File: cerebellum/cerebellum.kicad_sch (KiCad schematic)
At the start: 8 parts, among them J1 GPIO, U1 CAT24C256, U2 POLOLU_TB6612_CARRIER

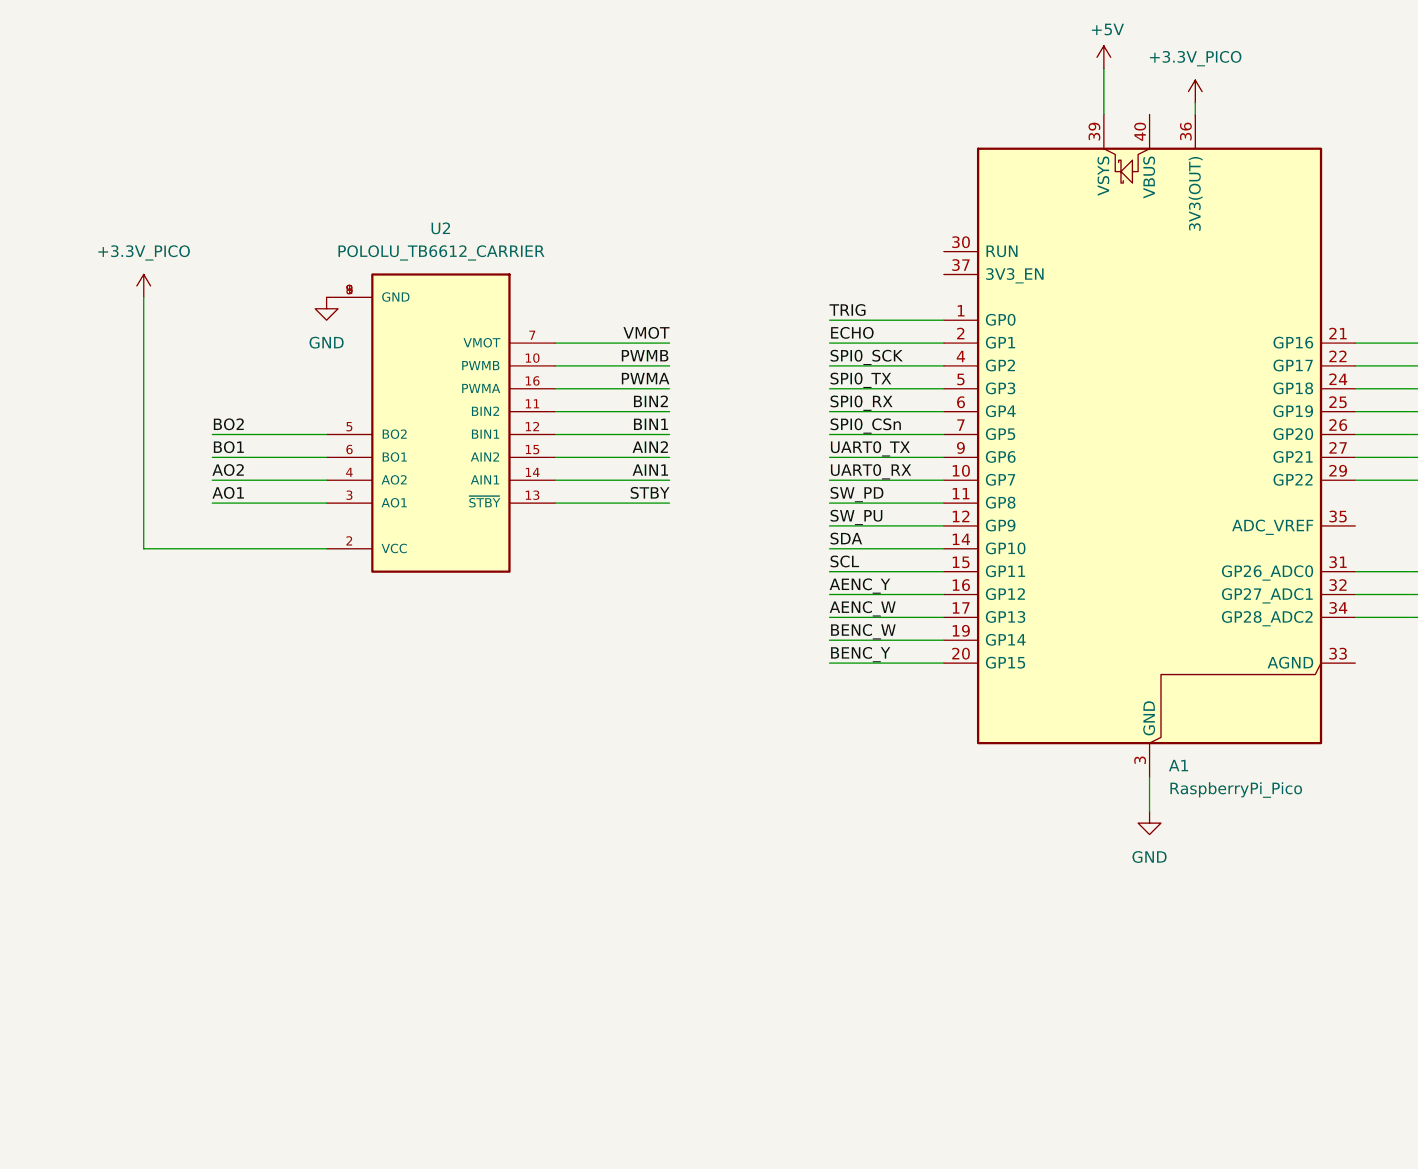
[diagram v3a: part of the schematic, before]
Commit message: update schematic
added HC-SR04
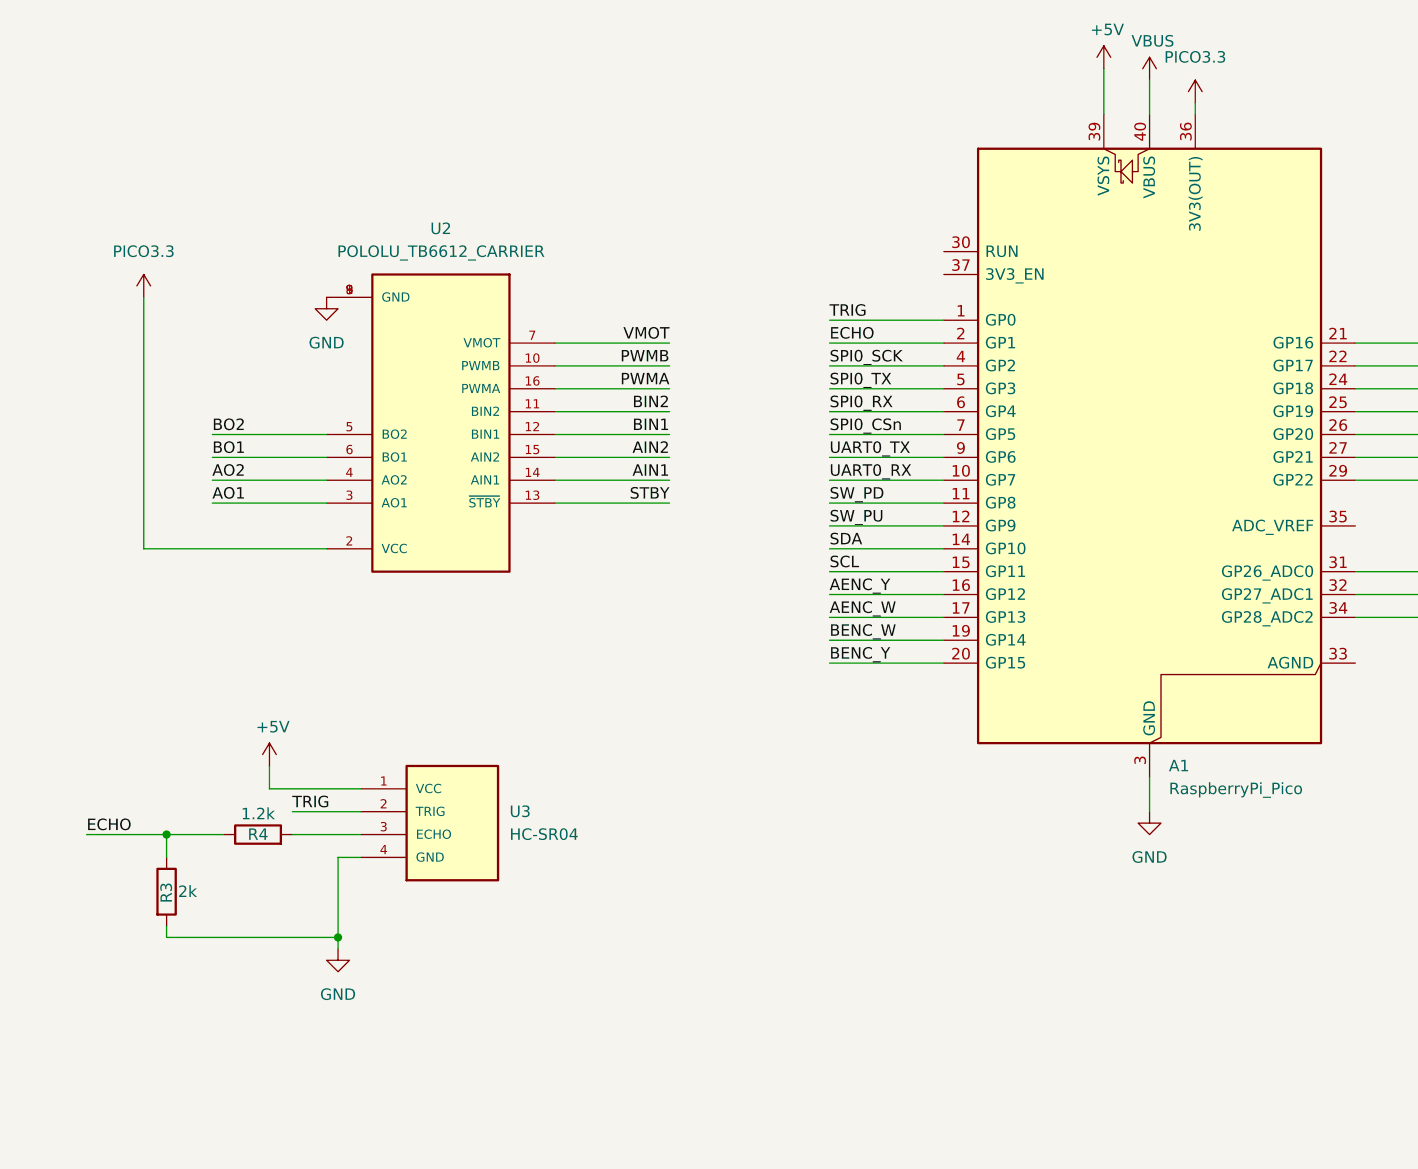
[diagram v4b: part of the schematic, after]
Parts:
- added R3: 2k, symbol Device:R
- added R4: 1.2k, symbol Device:R
- added U3: HC-SR04, HC-SR04:XCVR_HC-SR04, symbol HC-SR04:HC-SR04
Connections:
- net +5V: now also U3.1 (VCC)
- net ECHO: now also R3.1, R4.1
- net GND: now also R3.2, U3.4 (GND)
- net TRIG: now also U3.2 (TRIG)
- net VBUS: now reaches A1.40 (VBUS)
- net +3.3V_PICO renamed PICO3.3
- new net: R4.2, U3.3 (ECHO)

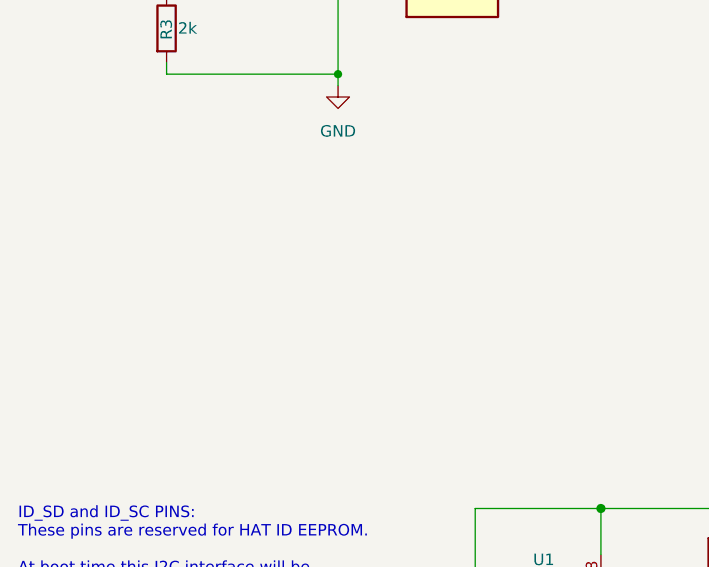
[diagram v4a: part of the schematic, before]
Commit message: update schematic
added RGB LED
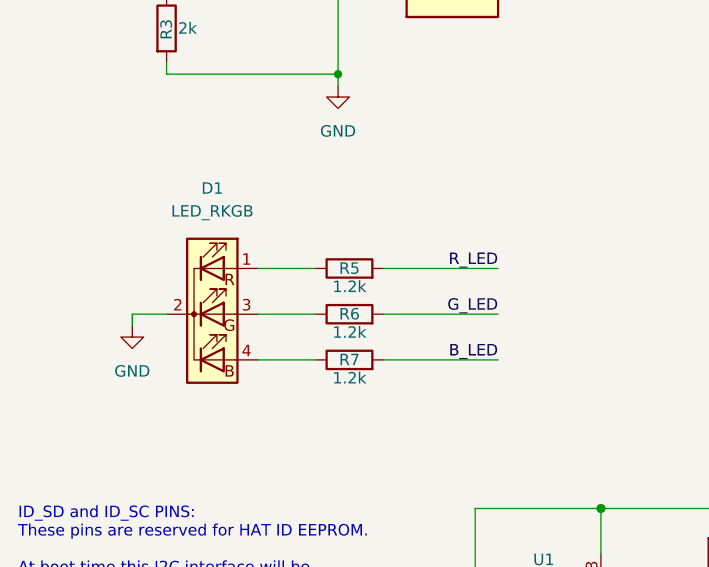
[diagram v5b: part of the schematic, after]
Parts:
- added D1: LED_RKGB, symbol Device:LED_RKGB
- added R5, R6, R7: 1.2k, symbol Device:R
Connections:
- net B_LED: now also R7.2
- net GND: now also D1.2 (K)
- net G_LED: now also R6.2
- net R_LED: now also R5.2
- new net: D1.1 (RA), R5.1
- new net: D1.3 (GA), R6.1
- new net: D1.4 (BA), R7.1

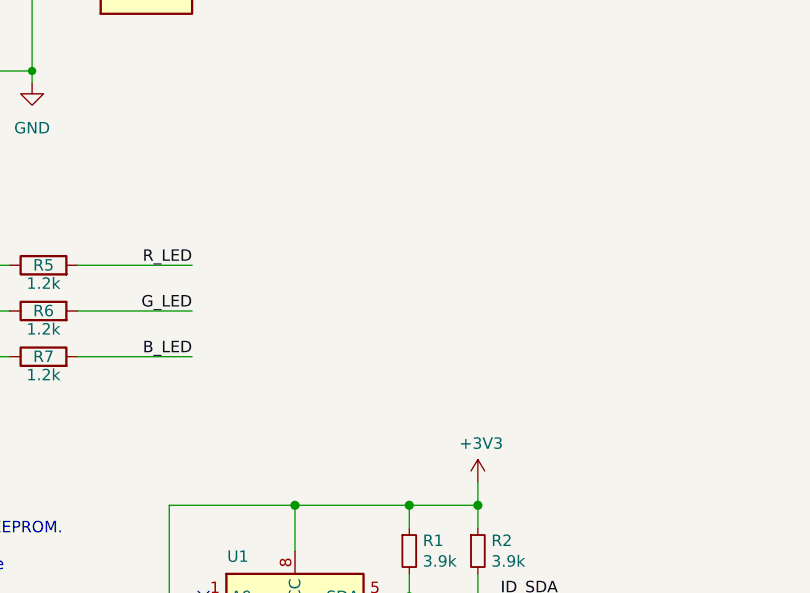
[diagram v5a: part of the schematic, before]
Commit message: update schematic
added pull-up and pull-down switches
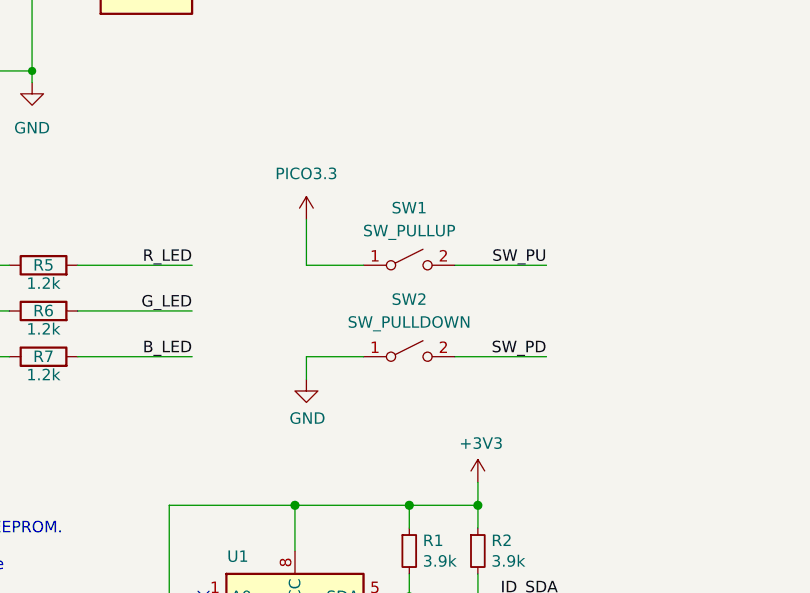
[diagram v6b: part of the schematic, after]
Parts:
- added SW1: SW_PULLUP, symbol Switch:SW_SPST
- added SW2: SW_PULLDOWN, symbol Switch:SW_SPST
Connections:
- net GND: now also SW2.1 (A)
- net PICO3.3: now also SW1.1 (A)
- net SW_PD: now also SW2.2 (B)
- net SW_PU: now also SW1.2 (B)

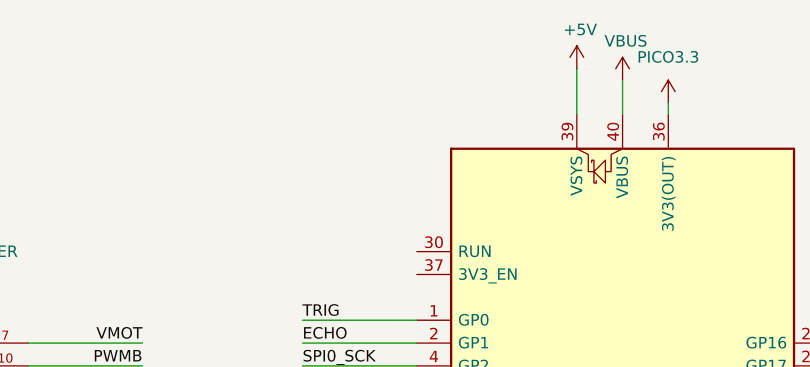
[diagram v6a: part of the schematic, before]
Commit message: update schematic
added spdt switch to power pico
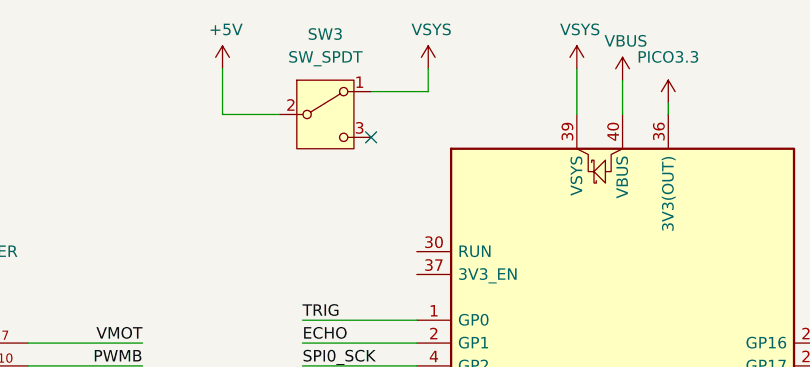
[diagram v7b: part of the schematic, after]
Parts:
- added SW3: SW_SPDT, symbol Switch:SW_SPDT
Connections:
- net +5V: now also SW3.2 (B); no longer A1.39 (VSYS)
- new net VSYS: A1.39 (VSYS), SW3.1 (A)
- no-connect marks 3 -> 4
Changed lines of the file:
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@@
 		(at 71.12 180.34)
 	)
+	(no_connect
+		(at 114.3 27.94)
+	)
 	(wire
 		(pts
@@
 	(wire
 		(pts
+			(xy 120.65 22.86) (xy 120.65 20.32)
+		)
+		(stroke
+			(width 0)
+			(type default)
+		)
+	)
+	(wire
+		(pts
 			(xy 147.32 25.4) (xy 147.32 24.13)
 		)
@@
 	(wire
 		(pts
+			(xy 97.79 25.4) (xy 104.14 25.4)
+		)
+		(stroke
+			(width 0)
+			(type default)
+		)
+	)
+	(wire
+		(pts
 			(xy 57.15 138.43) (xy 69.85 138.43)
 		)
@@
 	(wire
 		(pts
+			(xy 97.79 20.32) (xy 97.79 25.4)
+		)
+		(stroke
+			(width 0)
+			(type default)
+		)
+	)
+	(wire
+		(pts
 			(xy 248.92 68.58) (xy 246.38 68.58)
 		)
@@
 	(wire
 		(pts
+			(xy 114.3 22.86) (xy 120.65 22.86)
+		)
+		(stroke
+			(width 0)
+			(type default)
+		)
+	)
+	(wire
+		(pts
 			(xy 81.28 185.42) (xy 81.28 187.96)
 		)
@@
 	(symbol
 		(lib_id "power:+5V")
-		(at 137.16 20.32 0)
+		(at 97.79 20.32 0)
 		(unit 1)
 		(exclude_from_sim no)
@@
 		(dnp no)
 		(property "Reference" "#PWR011"
-			(at 137.16 24.13 0)
+			(at 97.79 24.13 0)
 			(effects
 				(font
@@
 		)
 		(property "Value" "+5V"
-			(at 137.5283 15.9956 0)
+			(at 98.1583 15.9956 0)
 			(effects
 				(font
@@
 		)
 		(property "Footprint" ""
-			(at 137.16 20.32 0)
+			(at 97.79 20.32 0)
 			(effects
 				(font
@@
 		)
 		(property "Datasheet" ""
-			(at 137.16 20.32 0)
+			(at 97.79 20.32 0)
 			(effects
 				(font
@@
 		)
 		(property "Description" ""
-			(at 137.16 20.32 0)
+			(at 97.79 20.32 0)
 			(effects
 				(font
@@
 	)
 	(symbol
+		(lib_id "power:+5V")
+		(at 120.65 20.32 0)
+		(unit 1)
+		(exclude_from_sim no)
+		(in_bom yes)
+		(on_board yes)
+		(dnp no)
+		(property "Reference" "#PWR020"
+			(at 120.65 24.13 0)
+			(effects
+				(font
+					(size 1.27 1.27)
+				)
+				(hide yes)
+			)
+		)
+		(property "Value" "VSYS"
+			(at 121.0183 15.9956 0)
+			(effects
+				(font
+					(size 1.27 1.27)
+				)
+			)
+		)
+		(property "Footprint" ""
+			(at 120.65 20.32 0)
+			(effects
+				(font
+					(size 1.27 1.27)
+				)
+			)
+		)
+		(property "Datasheet" ""
+			(at 120.65 20.32 0)
+			(effects
+				(font
+					(size 1.27 1.27)
+				)
+			)
+		)
+		(property "Description" ""
+			(at 120.65 20.32 0)
+			(effects
+				(font
+					(size 1.27 1.27)
+				)
+			)
+		)
+		(pin "1"
+		)
+		(instances
+			(project "cerebellum"
+				(path "/e63e39d7-6ac0-4ffd-8aa3-1841a4541b55"
+					(reference "#PWR020")
+					(unit 1)
+				)
+			)
+		)
+	)
+	(symbol
+		(lib_id "Switch:SW_SPDT")
+		(at 109.22 25.4 0)
+		(unit 1)
+		(exclude_from_sim no)
+		(in_bom yes)
+		(on_board yes)
+		(dnp no)
+		(fields_autoplaced yes)
+		(property "Reference" "SW3"
+			(at 109.22 16.51 0)
+			(effects
+				(font
+					(size 1.27 1.27)
+				)
+			)
+		)
+		(property "Value" "SW_SPDT"
+			(at 109.22 19.05 0)
+			(effects
+				(font
+					(size 1.27 1.27)
+				)
+			)
+		)
+		(property "Footprint" ""
+			(at 109.22 25.4 0)
+			(effects
+				(font
+					(size 1.27 1.27)
+				)
+				(hide yes)
+			)
+		)
+		(property "Datasheet" "~"
+			(at 109.22 33.02 0)
+			(effects
+				(font
+					(size 1.27 1.27)
+				)
+				(hide yes)
+			)
+		)
+		(property "Description" "Switch, single pole double throw"
+			(at 109.22 25.4 0)
+			(effects
+				(font
+					(size 1.27 1.27)
+				)
+				(hide yes)
+			)
+		)
+		(pin "2"
+		)
+		(pin "1"
+		)
+		(pin "3"
+		)
+		(instances
+			(project ""
+				(path "/e63e39d7-6ac0-4ffd-8aa3-1841a4541b55"
+					(reference "SW3")
+					(unit 1)
+				)
+			)
+		)
+	)
+	(symbol
 		(lib_name "GND_1")
 		(lib_id "power:GND")
@@
 					(unit 1)
 				)
+			)
+		)
+	)
+	(symbol
+		(lib_id "power:+5V")
+		(at 137.16 20.32 0)
+		(unit 1)
+		(exclude_from_sim no)
+		(in_bom yes)
+		(on_board yes)
+		(dnp no)
+		(property "Reference" "#PWR019"
+			(at 137.16 24.13 0)
+			(effects
+				(font
+					(size 1.27 1.27)
+				)
+				(hide yes)
+			)
+		)
+		(property "Value" "VSYS"
+			(at 137.5283 15.9956 0)
+			(effects
+				(font
+					(size 1.27 1.27)
+				)
+			)
+		)
+		(property "Footprint" ""
+			(at 137.16 20.32 0)
+			(effects
+				(font
+					(size 1.27 1.27)
+				)
+			)
+		)
+		(property "Datasheet" ""
+			(at 137.16 20.32 0)
+			(effects
+				(font
+					(size 1.27 1.27)
+				)
+			)
+		)
+		(property "Description" ""
+			(at 137.16 20.32 0)
+			(effects
+				(font
+					(size 1.27 1.27)
+				)
+			)
+		)
+		(pin "1"
+		)
+		(instances
+			(project "cerebellum"
+				(path "/e63e39d7-6ac0-4ffd-8aa3-1841a4541b55"
+					(reference "#PWR019")
+					(unit 1)
+				)
